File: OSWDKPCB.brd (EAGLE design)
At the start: 76.2 x 38.1 mm, 55 parts, among them IC1 S08AC60, IC2 S08JS16, IC3 BUFF, IC4 BUFF, IC7 NCP1117ST50T3G, P0 HDR-8, P1 HDR-8, P2 HDR-8, P3 HDR-8, U1 PMV160UP, U3 LP2985-33DBVR, Y1 4MHz, Y2 12MHz

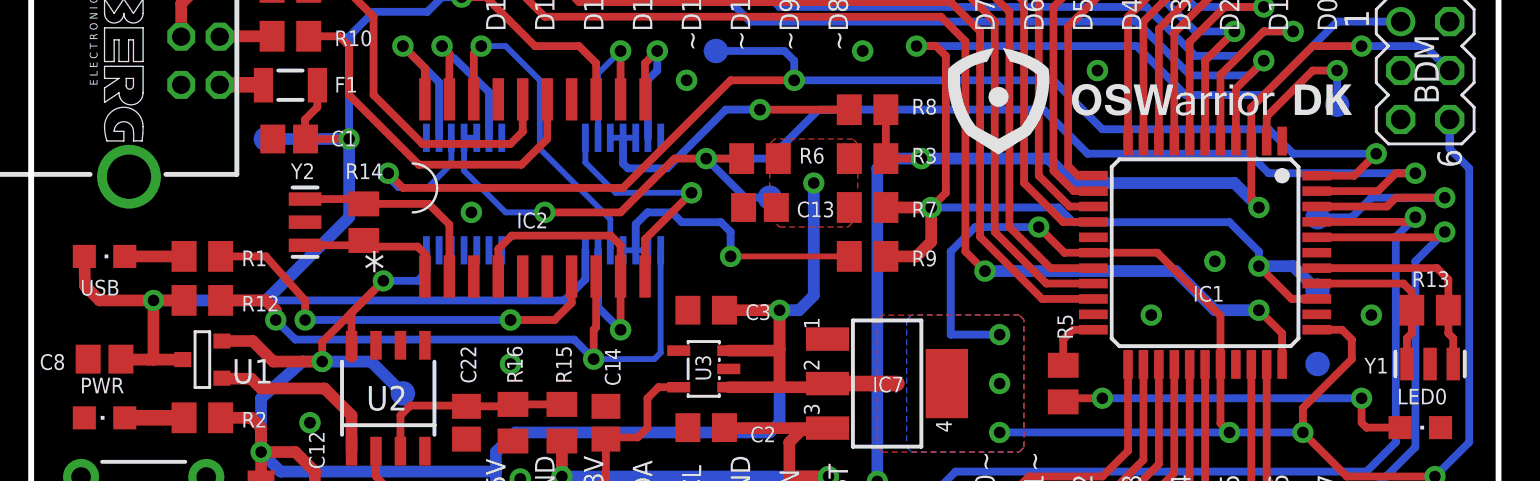
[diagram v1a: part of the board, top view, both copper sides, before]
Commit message: VCC de los buffer
La alimentación de ambos buffers se ha cambiado a 5V de la tarjeta.
El logo de la parte trasera se ha actualizado a un simbolo.
La revision ha cambiado a 4.00
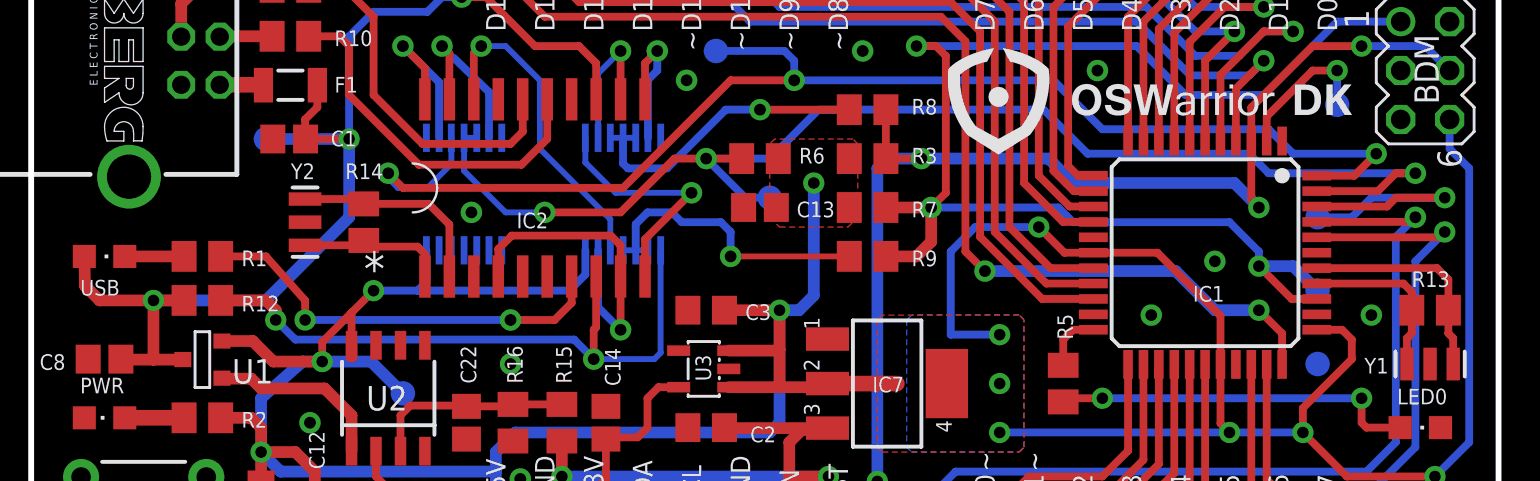
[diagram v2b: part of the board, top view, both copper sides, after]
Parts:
- added U$2: OSWDK_BACK_LOGO, OSWarrior:OSWDK_BACK_LOGO
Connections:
- net +5V: now also IC4.14
- net USBVCC: no longer IC4.14
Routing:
- net USBVCC: track 80.0 -> 61.4 mm
- net +5V: track 188.2 -> 195.0 mm
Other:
- board text added: "Board Model: OSWarrior DK Revision: 4.00 Open-Source Hardware www.oswarrior.com Hecho en México"
- board text removed: "Board Model: OSWarrior DK Revision: 3.00 Open-Source Hardware www.oswarrior.com Hecho en México"

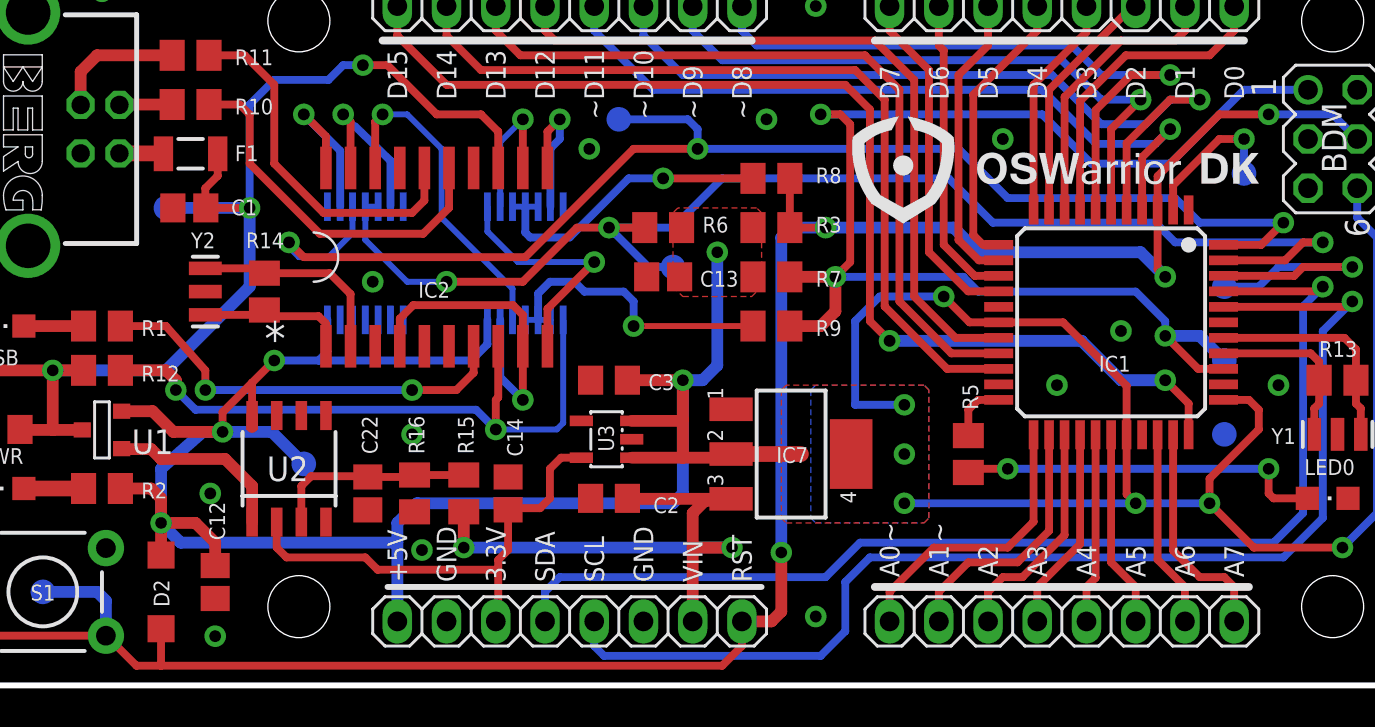
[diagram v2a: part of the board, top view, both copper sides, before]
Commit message: Silkscreen update.
This was the last update before the manufcaturing process, this update
only imprive the logo mark on the PCB, it doesnt have any layout
changes.
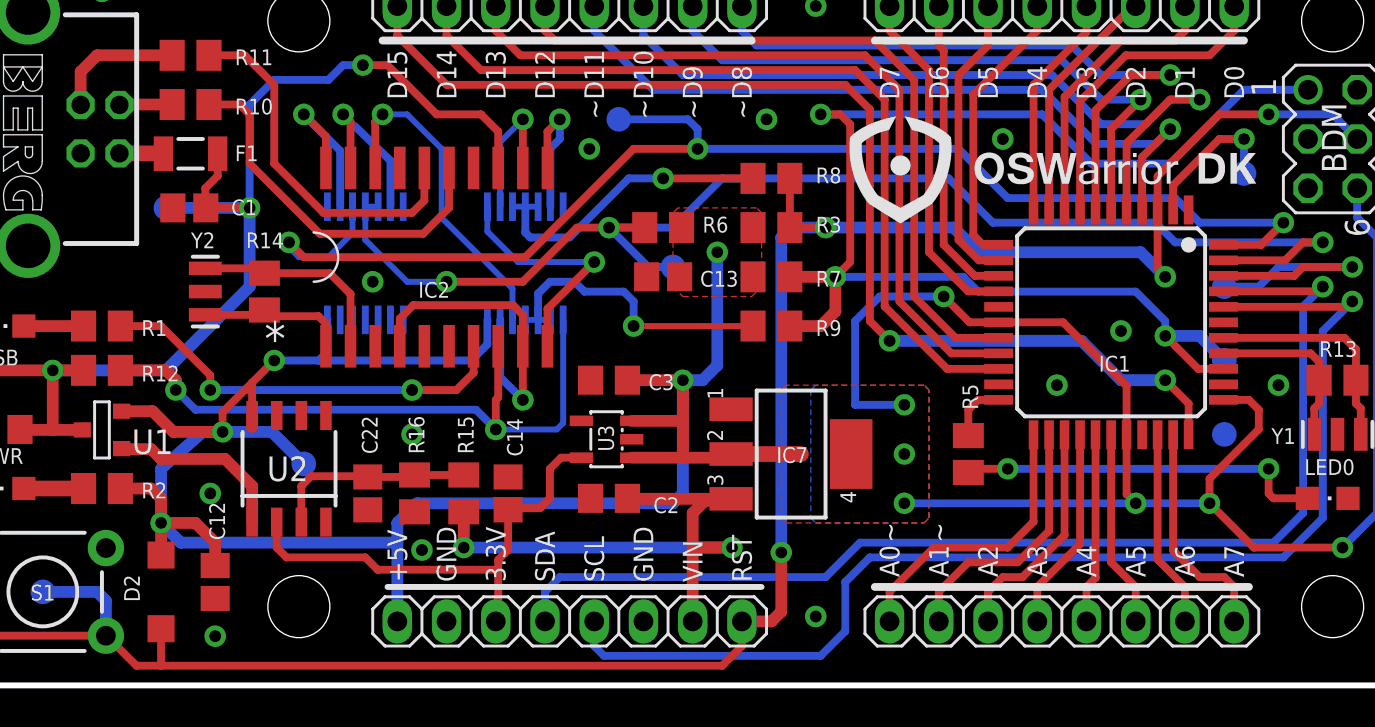
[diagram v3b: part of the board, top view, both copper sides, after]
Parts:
- moved U$2 0.25 mm to (33.0, 19.3)
- moved U$1 0.14 mm to (58.5, 25.9)
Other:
- board text added: "Board Model: OSWDK Revision: 4.00 Open-Source Hardware www.oswarrior.com Hecho en México"
- board text removed: "Board Model: OSWarrior DK Revision: 4.00 Open-Source Hardware www.oswarrior.com Hecho en México"
- board text removed: "OSWarrior Dark Knight"
- board text removed: "V3.0 Rev1.0"
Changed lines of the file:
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@@
 <setting verticaltext="up"/>
 </settings>
-<grid distance="0.00001" unitdist="inch" unit="inch" style="lines" multiple="1" display="yes" altdistance="0.025" altunitdist="inch" altunit="inch"/>
+<grid distance="0.01" unitdist="inch" unit="inch" style="lines" multiple="1" display="yes" altdistance="0.025" altunitdist="inch" altunit="inch"/>
 <layers>
 <layer number="1" name="Top" color="12" fill="1" visible="yes" active="yes"/>
@@
 <text x="37.338" y="5.334" size="1.016" layer="25" rot="R90">GND</text>
 <text x="39.878" y="5.334" size="1.016" layer="25" rot="R90">VIN</text>
-<text x="66.2305" y="12.192" size="2.1844" layer="26" rot="MR0">OSWarrior Dark Knight</text>
-<text x="66.2305" y="9.652" size="1.4224" layer="26" rot="MR0">V3.0 Rev1.0</text>
 <text x="34.798" y="5.334" size="1.016" layer="25" rot="R90">SCL</text>
 <text x="32.258" y="5.334" size="1.016" layer="25" rot="R90">SDA</text>
@@
 <text x="27.178" y="5.334" size="1.016" layer="25" rot="R90">GND</text>
 <text x="29.718" y="5.334" size="1.016" layer="25" rot="R90">3.3V</text>
-<text x="74.399140625" y="21.3741" size="0.8128" layer="22" font="vector" rot="MR0" align="top-left">Board Model: OSWarrior DK
+<text x="74.399140625" y="21.3741" size="0.8128" layer="22" font="vector" rot="MR0" align="top-left">Board Model: OSWDK
 Revision: 4.00
 Open-Source Hardware
@@
 <element name="IC2" library="OSWarrior" package="SOIC-20" value="S08JS16" x="26.162" y="22.098" smashed="yes">
 <attribute name="NAME" x="25.2095" y="20.0025" size="0.8128" layer="25"/>
-<attribute name="VALUE" x="22.483571875" y="21.356065625" size="1.4224" layer="27"/>
+<attribute name="VALUE" x="22.200871875" y="21.42693125" size="1.4224" layer="27"/>
 </element>
 <element name="R3" library="resistor" package="M0805" value="10K" x="43.434" y="23.622" smashed="yes">
@@
 </element>
 <element name="D2" library="diode" package="SOD123" value="CD1206-S01575" x="11.938" y="4.826" smashed="yes" rot="R270">
-<attribute name="NAME" x="11.557" y="5.461" size="0.8128" layer="25" rot="R270"/>
+<attribute name="NAME" x="10.033" y="5.715" size="0.8128" layer="25" rot="R270"/>
 </element>
 <element name="U1" library="PMV160UP" package="SOT-23" value="PMV160UP" x="8.89" y="13.208" smashed="yes" rot="R270">
@@
 <attribute name="VALUE" x="68.199" y="29.464" size="1.27" layer="27" ratio="10" rot="R270"/>
 </element>
-<element name="U$1" library="OSWarrior" package="OSWDK_LOGO" value="OSWDK_LOGO" x="58.674" y="25.908"/>
-<element name="U$2" library="OSWarrior" package="OSWDK_BACK_LOGO" value="OSWDK_BACK_LOGO" x="33.02" y="19.05"/>
+<element name="U$1" library="OSWarrior" package="OSWDK_LOGO" value="OSWDK_LOGO" x="58.532775" y="25.908"/>
+<element name="U$2" library="OSWarrior" package="OSWDK_BACK_LOGO" value="OSWDK_BACK_LOGO" x="33.02" y="19.304"/>
 </elements>
 <signals>
@@
 <contactref element="IC2" pad="7"/>
 <contactref element="R1" pad="1"/>
-<wire x1="9.84" y1="18.542" x2="12.192" y2="18.542" width="0.4064" layer="1"/>
-<via x="14.224" y="15.24" extent="1-16" drill="0.6" diameter="1.016"/>
-<wire x1="14.224" y1="15.24" x2="24.892" y2="15.24" width="0.4064" layer="16"/>
+<wire x1="9.84" y1="18.542" x2="11.938" y2="18.542" width="0.4064" layer="1"/>
+<via x="14.478" y="15.24" extent="1-16" drill="0.6" diameter="1.016"/>
+<wire x1="14.478" y1="15.24" x2="24.892" y2="15.24" width="0.4064" layer="16"/>
 <via x="24.892" y="15.24" extent="1-16" drill="0.6096" diameter="1.016"/>
 <wire x1="24.892" y1="15.24" x2="27.178" y2="15.24" width="0.4064" layer="1"/>
 <wire x1="27.178" y1="15.24" x2="28.067" y2="16.129" width="0.4064" layer="1"/>
 <wire x1="28.067" y1="16.129" x2="28.067" y2="17.498" width="0.4064" layer="1"/>
-<wire x1="12.192" y1="18.542" x2="14.224" y2="16.256" width="0.4064" layer="1"/>
-<wire x1="14.224" y1="16.256" x2="14.224" y2="15.24" width="0.4064" layer="1"/>
+<wire x1="11.938" y1="18.542" x2="14.478" y2="16.002" width="0.4064" layer="1"/>
+<wire x1="14.478" y1="16.002" x2="14.478" y2="15.24" width="0.4064" layer="1"/>
 </signal>
 <signal name="N$1">

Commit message: Version 4.2
Revision 3.0
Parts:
- added BDM_EN: (no value), jumper:SJ
- renumbered TP_BKGD to TP_BKGD1
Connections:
- new net N$6: BDM_EN.2, IC1.36, TP_BKGD1.TP
- net BKGD: now also BDM_EN.1; no longer IC1.36, TP_BKGD1.TP
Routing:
- net BKGD: track 70.5 -> 56.0 mm, vias 3 -> 2
- net N$6: track 0.00 -> 13.1 mm, vias 0 -> 1
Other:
- board text added: "Equipo OSWarrior: - Hugo Arganda (hugo.arganda@oswarrior.com) - Daniel Castellon (daniel.castellon@oswarrior.com) - Isaac Avila (isaac.avila@oswarrior.com)"
- board text added: "Los diseños son proporcionados "como son" y "con todos sus errores". El equipo de OSWarrior no se hace responsable por el uso o manejo de estos archivos asi como su reproducción total o parcial e incluso la venta de los productos derivados de este diseño. El equipo de OSWarrior podría hacer cambios en las especificaciones y descripciones del producto en cualquier momento sin previo aviso. OSWarri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"
- board text added: "Released under the Creative Commons Attribution Share-Alike 3.0 License"
- board text added: "http://creativecommons.org/licenses/by-sa/3.0"
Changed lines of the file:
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@@
 <wire x1="74.44231875" y1="12.26311875" x2="56.63056875" y2="12.26311875" width="0.254" layer="22"/>
 <wire x1="56.63056875" y1="12.26311875" x2="56.63056875" y2="12.24153125" width="0.254" layer="22"/>
+<text x="78.486" y="22.606" size="1.143" layer="21" font="vector" ratio="12" align="top-left">Equipo OSWarrior:
+- Hugo Arganda (hugo.arganda@oswarrior.com)
+- Daniel Castellon (daniel.castellon@oswarrior.com)
+- Isaac Avila (isaac.avila@oswarrior.com)</text>
+<text x="-2.54" y="42.672" size="1.778" layer="21">Released under the Creative Commons Attribution Share-Alike 3.0 License</text>
+<text x="13.462" y="39.878" size="1.778" layer="21">http://creativecommons.org/licenses/by-sa/3.0</text>
+<text x="0" y="-3.302" size="1.6764" layer="21" align="top-left">Los diseños son proporcionados "como son" y "con todos sus errores".
+El equipo de OSWarrior no se hace responsable por el uso o manejo de
+estos archivos asi como su reproducción total o parcial e incluso
+la venta de los productos derivados de este diseño.
+El equipo de OSWarrior podría hacer cambios en las especificaciones y
+descripciones del producto en cualquier momento sin previo aviso.
+OSWarrior es una marca registrada.</text>
 </plain>
 <attributes>
@@
 <attribute name="MF" value="" x="5.08" y="28.702" size="1.778" layer="27" rot="R270" display="off"/>
 <attribute name="OC_FARNELL" value="unknown" x="5.08" y="28.702" size="1.778" layer="27" rot="R270" display="off"/>
-<attribute name="VALUE" x="2.667" y="25.908" size="1.27" layer="27" rot="R90"/>
+<attribute name="VALUE" x="5.715" y="26.162" size="1.27" layer="27" rot="R90"/>
 </element>
 <element name="Y1" library="SparkFun" package="RESONATOR-SMD" value="4MHz" x="72.644" y="12.954" smashed="yes">
@@
 <element name="R11" library="resistor" package="M0805" value="33" x="13.462" y="32.512" smashed="yes">
 <attribute name="NAME" x="15.748" y="32.004" size="0.8128" layer="25"/>
-</element>
-<element name="TP_BKGD" library="testpad" package="B1,27" value="PTR1B1,27" x="66.802" y="16.764" smashed="yes" rot="MR0">
-<attribute name="TP_SIGNAL_NAME" value="" x="67.437" y="14.859" size="1" layer="38" rot="MR0"/>
 </element>
 <element name="TP_RST" library="testpad" package="B1,27" value="PTR1B1,27" x="5.842" y="4.826" smashed="yes" rot="MR0">
@@
 <element name="U$1" library="OSWarrior" package="OSWDK_LOGO" value="OSWDK_LOGO" x="58.532775" y="25.908"/>
 <element name="U$2" library="OSWarrior" package="OSWDK_BACK_LOGO" value="OSWDK_BACK_LOGO" x="33.02" y="19.304"/>
+<element name="BDM_EN" library="jumper" package="SJ" value="" x="58.674" y="20.32" rot="MR180"/>
+<element name="TP_BKGD1" library="testpad" package="B1,27" value="PTR1B1,27" x="66.802" y="16.764" rot="MR0">
+<attribute name="TP_SIGNAL_NAME" value="" x="66.802" y="16.764" size="1.778" layer="28" rot="MR0" display="off"/>
+</element>
 </elements>
 <signals>
@@
 </signal>
 <signal name="BKGD">
-<contactref element="IC1" pad="36"/>
 <contactref element="R7" pad="1"/>
 <contactref element="R9" pad="1"/>
-<wire x1="66.76" y1="16.3325" x2="65.4555" y2="16.3325" width="0.4064" layer="1"/>
 <via x="46.736" y="21.082" extent="1-16" drill="0.6096" diameter="1.016"/>
 <wire x1="46.736" y1="21.082" x2="53.34" y2="21.082" width="0.4064" layer="16"/>
@@
 <wire x1="46.99" y1="29.464" x2="45.974" y2="29.464" width="0.4064" layer="1"/>
 <contactref element="BDM" pad="1"/>
-<contactref element="TP_BKGD" pad="TP"/>
-<wire x1="65.532" y1="18.034" x2="66.802" y2="16.764" width="0.6096" layer="16"/>
 <wire x1="64.008" y1="26.924" x2="67.818" y2="30.734" width="0.4064" layer="16"/>
 <wire x1="67.818" y1="30.734" x2="71.12" y2="30.734" width="0.4064" layer="16"/>
-<wire x1="65.4555" y1="16.3325" x2="63.754" y2="18.034" width="0.4064" layer="1"/>
-<via x="63.754" y="18.034" extent="1-16" drill="0.6" diameter="1.016"/>
-<wire x1="63.754" y1="18.034" x2="65.532" y2="18.034" width="0.6096" layer="16"/>
-<wire x1="62.23" y1="20.32" x2="54.102" y2="20.32" width="0.4064" layer="16"/>
-<wire x1="62.23" y1="20.32" x2="63.754" y2="18.796" width="0.4064" layer="16"/>
-<wire x1="63.754" y1="18.796" x2="63.754" y2="18.034" width="0.4064" layer="16"/>
+<contactref element="BDM_EN" pad="1"/>
+<wire x1="57.912" y1="20.32" x2="54.102" y2="20.32" width="0.4064" layer="16"/>
 </signal>
 <signal name="RESET">
@@
 <wire x1="29.933" y1="9.144" x2="29.845" y2="9.056" width="0.4064" layer="1"/>
 </signal>
+<signal name="N$6">
+<contactref element="TP_BKGD1" pad="TP"/>
+<contactref element="IC1" pad="36"/>
+<contactref element="BDM_EN" pad="2"/>
+<wire x1="59.436" y1="20.32" x2="62.23" y2="20.32" width="0.4064" layer="16"/>
+<via x="63.754" y="18.034" extent="1-16" drill="0.6096" diameter="1.1176"/>
+<wire x1="63.754" y1="18.034" x2="65.2015" y2="16.3325" width="0.4064" layer="1"/>
+<wire x1="65.2015" y1="16.3325" x2="66.76" y2="16.3325" width="0.4064" layer="1"/>
+<wire x1="66.802" y1="16.764" x2="65.532" y2="18.034" width="0.4064" layer="16"/>
+<wire x1="65.532" y1="18.034" x2="63.754" y2="18.034" width="0.4064" layer="16"/>
+<wire x1="62.23" y1="20.32" x2="63.754" y2="18.796" width="0.4064" layer="16"/>
+<wire x1="63.754" y1="18.796" x2="63.754" y2="18.034" width="0.4064" layer="16"/>
+</signal>
 </signals>
